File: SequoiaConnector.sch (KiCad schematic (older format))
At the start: 5 parts, among them U1 molex_impact_85ohm_left_and_r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

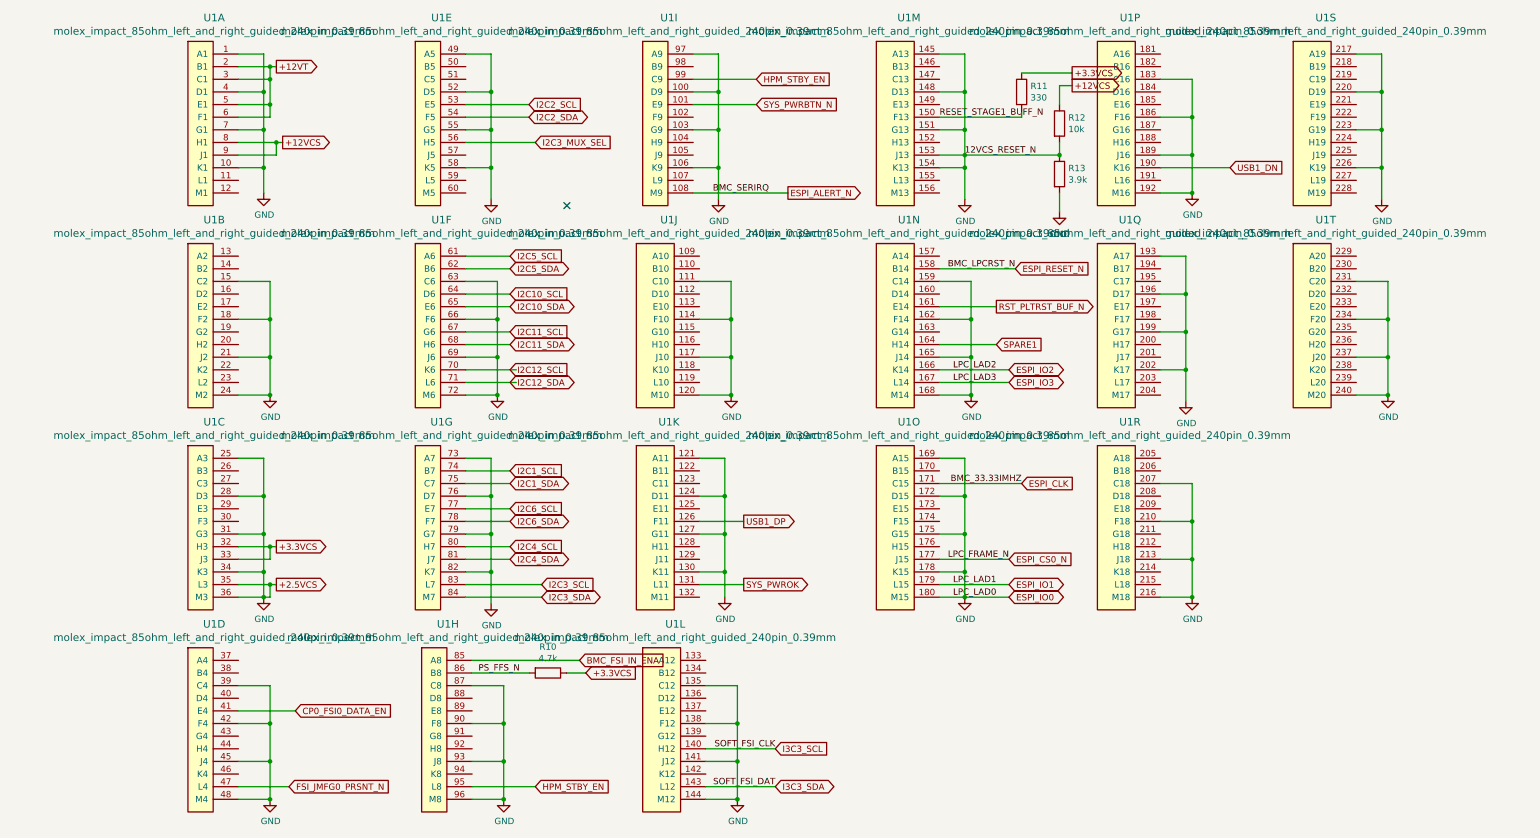
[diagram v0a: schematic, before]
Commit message: Removed extra junctions that were shorting 2.5v to gnd.
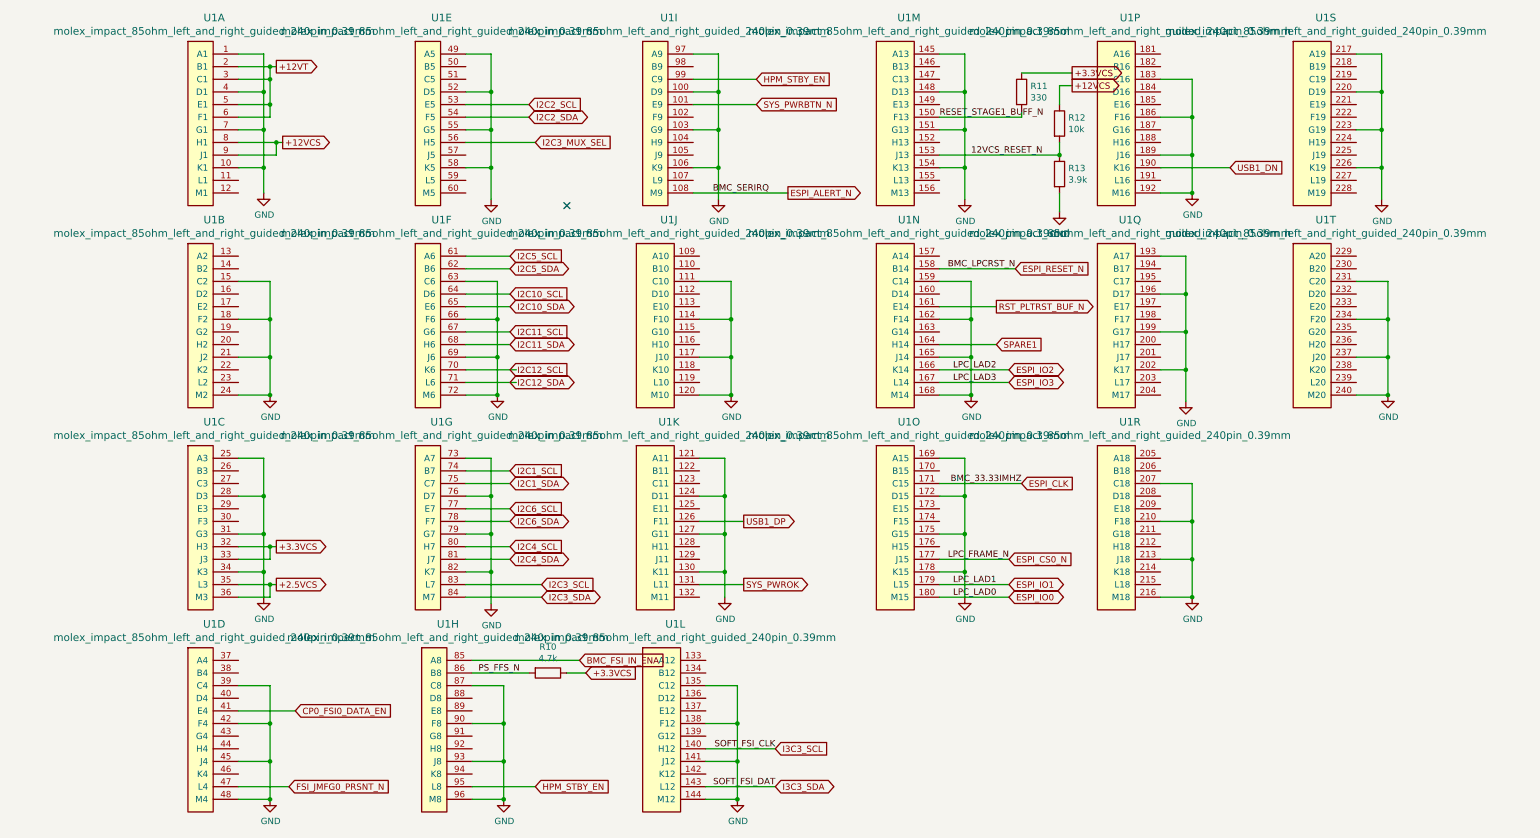
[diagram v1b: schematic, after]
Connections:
- net GND: no longer R12.2, R13.1, U1.153 (J13), U1.180 (M15), U1.35 (L3), U1.36 (M3)
- new net +2.5VCS: U1.35 (L3), U1.36 (M3)
- new net 12VCS_RESET_N: R12.2, R13.1, U1.153 (J13)
- new net ESPI_IO0: U1.180 (M15)
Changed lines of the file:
@@
 Wire Wire Line
 	8000 2350 8000 2500
-Text Label 7250 2050 0    50   ~ 0
+Text Label 7300 2050 0    50   ~ 0
 12VCS_RESET_N
 Text GLabel 4250 6150 2    50   Input ~ 0
@@
 Wire Wire Line
 	7050 1750 7700 1750
-Wire Wire Line
-	7050 2050 7250 2050
 Text GLabel 7600 5450 2    50   BiDi ~ 0
 ESPI_IO1
@@
 Wire Wire Line
 	9000 3750 9000 3450
-Wire Wire Line
-	7050 5550 7250 5550
 $Comp
 L power:GND #PWR023
@@
 	7050 3950 7300 3950
 Connection ~ 7300 3950
-Wire Wire Line
-	7250 2150 7250 2050
 Connection ~ 7250 2150
 Wire Wire Line
@@
 Wire Wire Line
 	7250 2150 7250 2400
-Connection ~ 7250 2050
-Wire Wire Line
-	7250 2050 8000 2050
-Wire Wire Line
-	7250 2050 7250 1850
 Text GLabel 5750 6750 2    50   Input ~ 0
 I3C3_SCL
@@
 Wire Wire Line
 	7250 5350 7250 5050
-Connection ~ 7250 5550
-Wire Wire Line
-	7250 5550 7600 5550
 Wire Wire Line
 	10550 1250 10350 1250
@@
 	1500 5450 1750 5450
 Wire Wire Line
-	1500 5550 1700 5550
-Wire Wire Line
 	1750 5550 1750 5450
-Connection ~ 1700 5550
-Wire Wire Line
-	1700 5550 1750 5550
 Connection ~ 1750 5450
 Wire Wire Line
@@
 Wire Wire Line
 	3650 4650 3300 4650
+Wire Wire Line
+	1500 5550 1750 5550
+Wire Wire Line
+	7050 5550 7600 5550
+Wire Wire Line
+	7050 2050 8000 2050
+Wire Wire Line
+	7250 1850 7250 2150
 $EndSCHEMATC
